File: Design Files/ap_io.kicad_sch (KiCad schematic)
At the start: 9 parts, among them J16 Conn_01x06_MountingPin, J17 Conn_01x06_MountingPin, J18 Conn_01x06_MountingPin, J19 Conn_01x06_MountingPin, U18 PCA9685PW

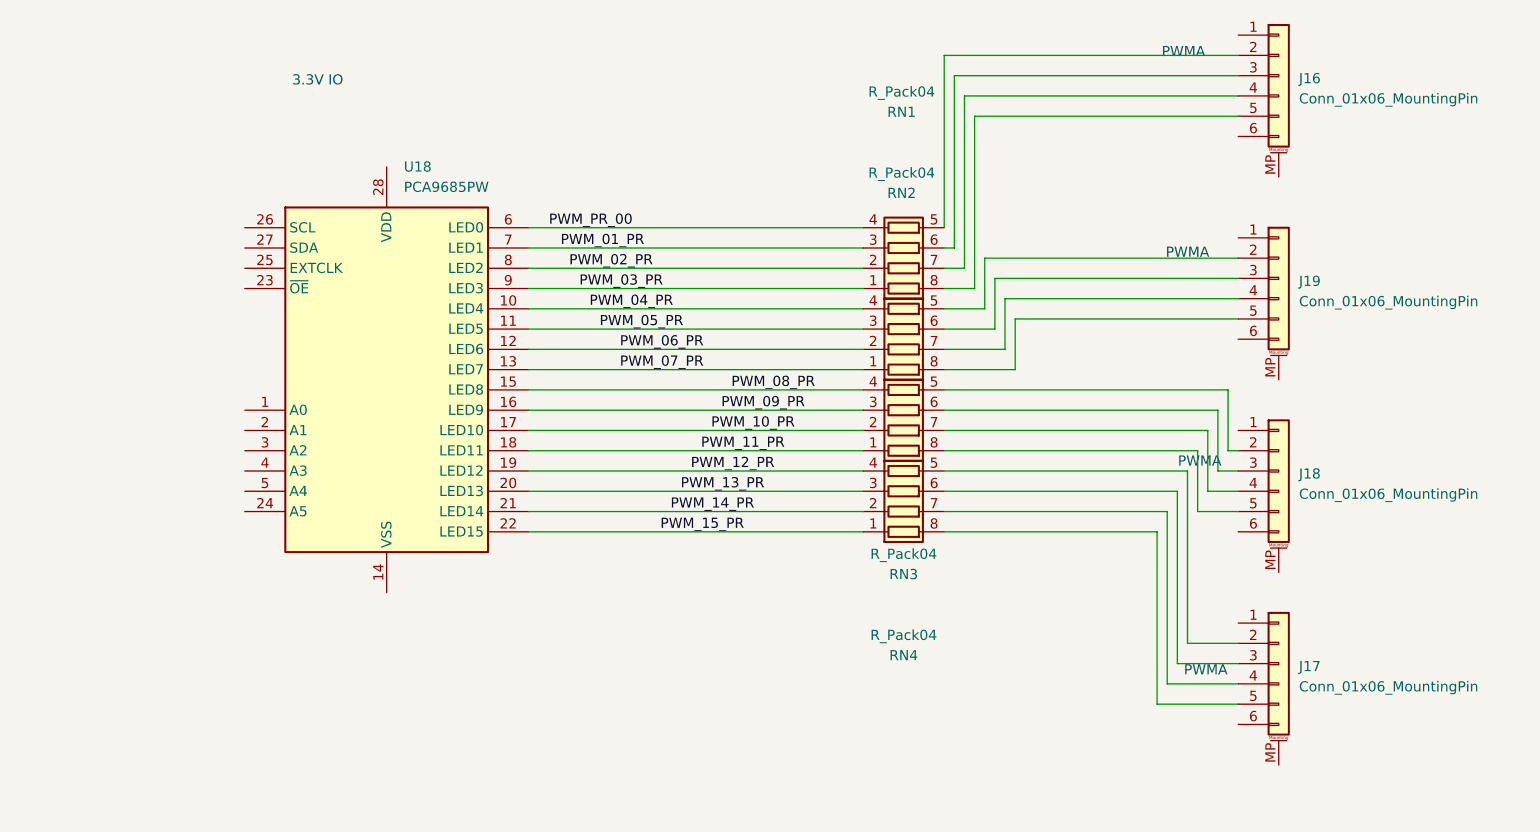
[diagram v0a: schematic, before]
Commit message: Fixed power & GPIO nets
Added PWM I2C Bus
Replaced global power labels on the sensor page with hierarchical pins & page labels
Cleaned up CM5 GPIO block sheet
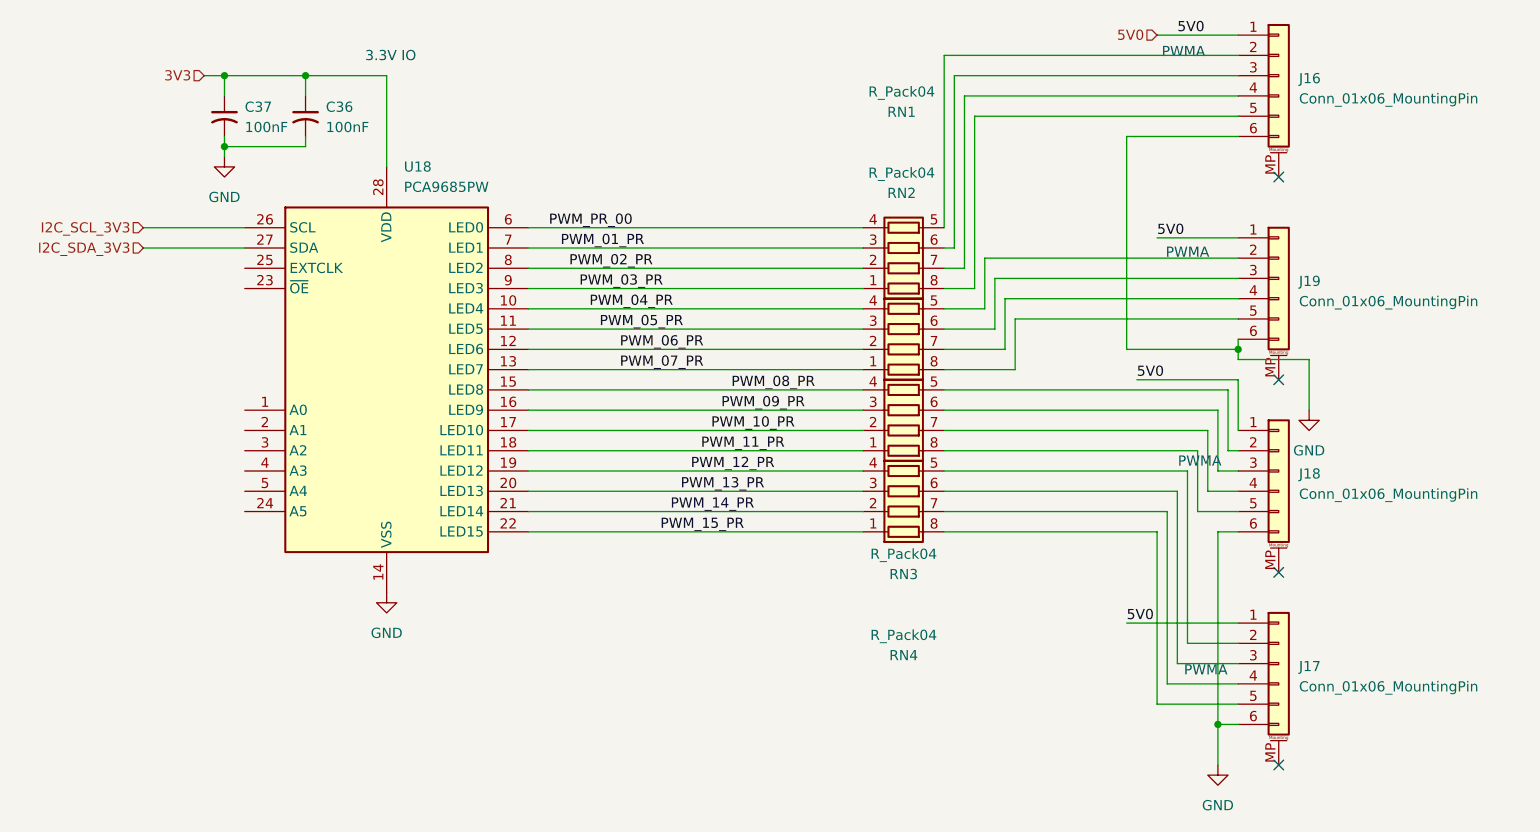
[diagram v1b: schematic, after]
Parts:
- added C36, C37: 100nF, Capacitor_SMD:C_0402_1005Metric, symbol Device:C_Small_US
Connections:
- net 5V0: now reaches J18.1 (Pin_1)
- net 5V0: now also J16.1 (Pin_1), J17.1 (Pin_1), J19.1 (Pin_1)
- net GND: now reaches J18.6 (Pin_6)
- net GND: now also J16.6 (Pin_6), J17.6 (Pin_6), J19.6 (Pin_6), U18.14 (VSS), C36.2, C37.2
- net I2C_SCL_3V3: now reaches U18.26 (SCL)
- net I2C_SDA_3V3: now reaches U18.27 (SDA)
- net 3V3: now reaches U18.28 (VDD)
- net 3V3: now also C36.1, C37.1
- no-connect marks 0 -> 4

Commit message: Misc
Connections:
- net PWM_PR_00 renamed PWM_00_PR
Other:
- note removed: "PWMA"
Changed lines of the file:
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@@
 		(comment 3 "https://github.com/loganrf/compactPi")
-	)
-	(text "PWMA"
-		(exclude_from_sim no)
-		(at 246.634 110.744 0)
-		(effects
-			(font
-				(size 1.27 1.27)
-			)
-		)
 	)
 	(text "3.3V IO"
@@
 		)
 	)
-	(text "PWMA"
-		(exclude_from_sim no)
-		(at 247.396 136.906 0)
-		(effects
-			(font
-				(size 1.27 1.27)
-			)
-		)
-	)
-	(text "PWMA"
-		(exclude_from_sim no)
-		(at 245.11 84.582 0)
-		(effects
-			(font
-				(size 1.27 1.27)
-			)
-		)
-	)
-	(text "PWMA"
-		(exclude_from_sim no)
-		(at 244.602 59.436 0)
-		(effects
-			(font
-				(size 1.27 1.27)
-			)
-		)
-	)
 	(junction
 		(at 251.46 96.52)
@@
 		)
 	)
-	(label "PWM_PR_00"
+	(label "PWM_00_PR"
 		(at 165.1 81.28 0)
 		(effects
